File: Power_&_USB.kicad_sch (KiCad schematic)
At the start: 36 parts, among them J1 UJ20-C-H-G-SMT-1-P16-TR, U1 TPS62840YBGR, U2 TPS62840YBGR, U4 FT232HPQ

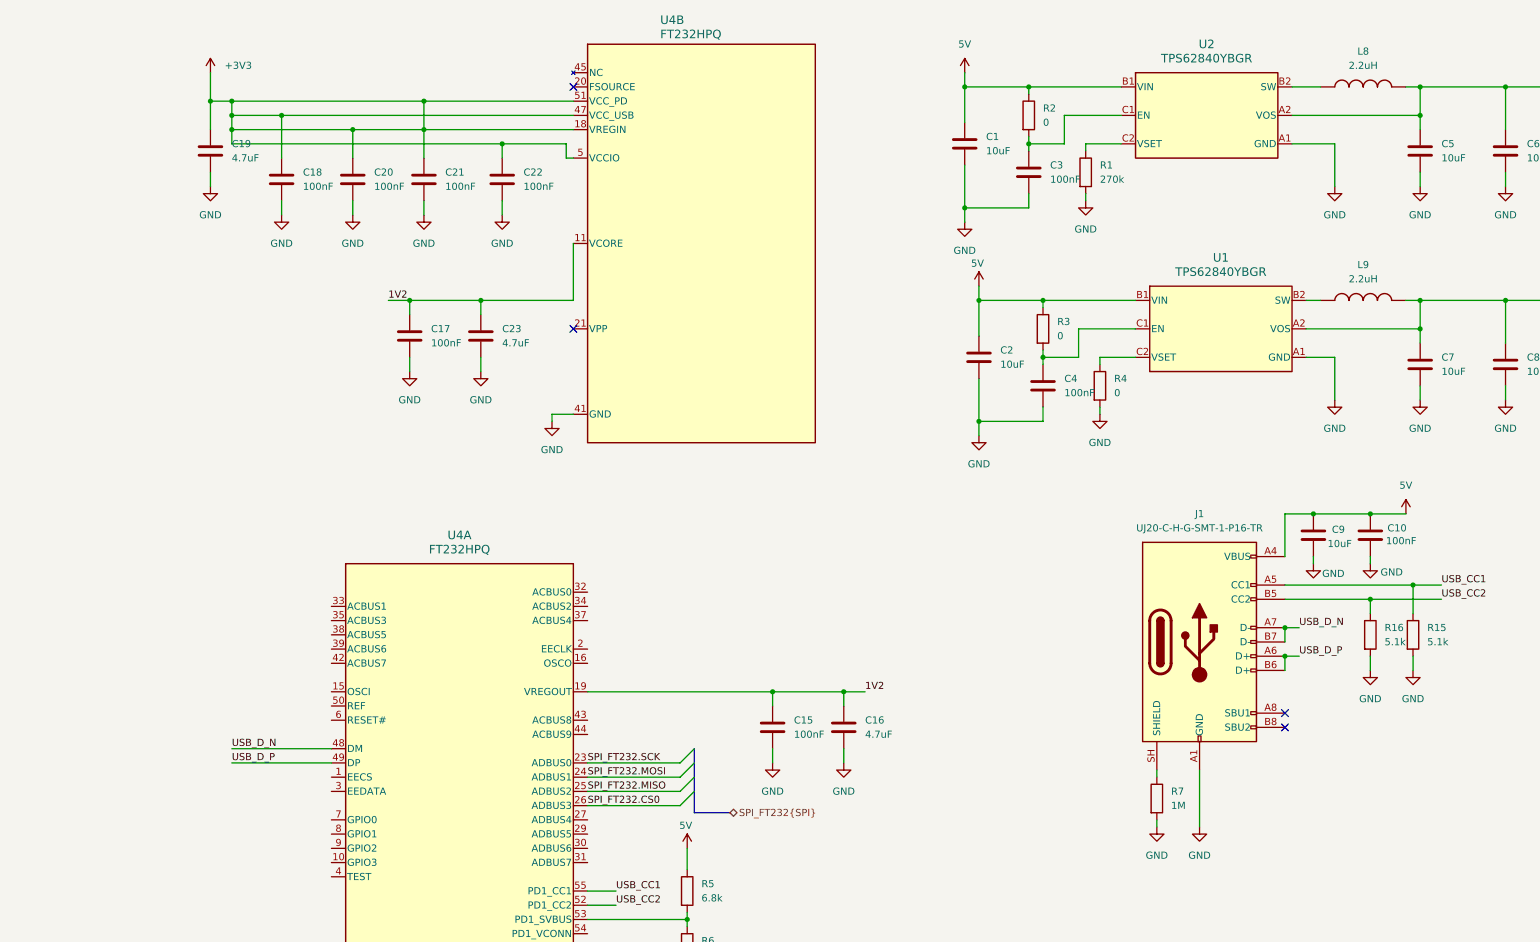
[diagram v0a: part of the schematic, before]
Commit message: added schematics comments of review 1
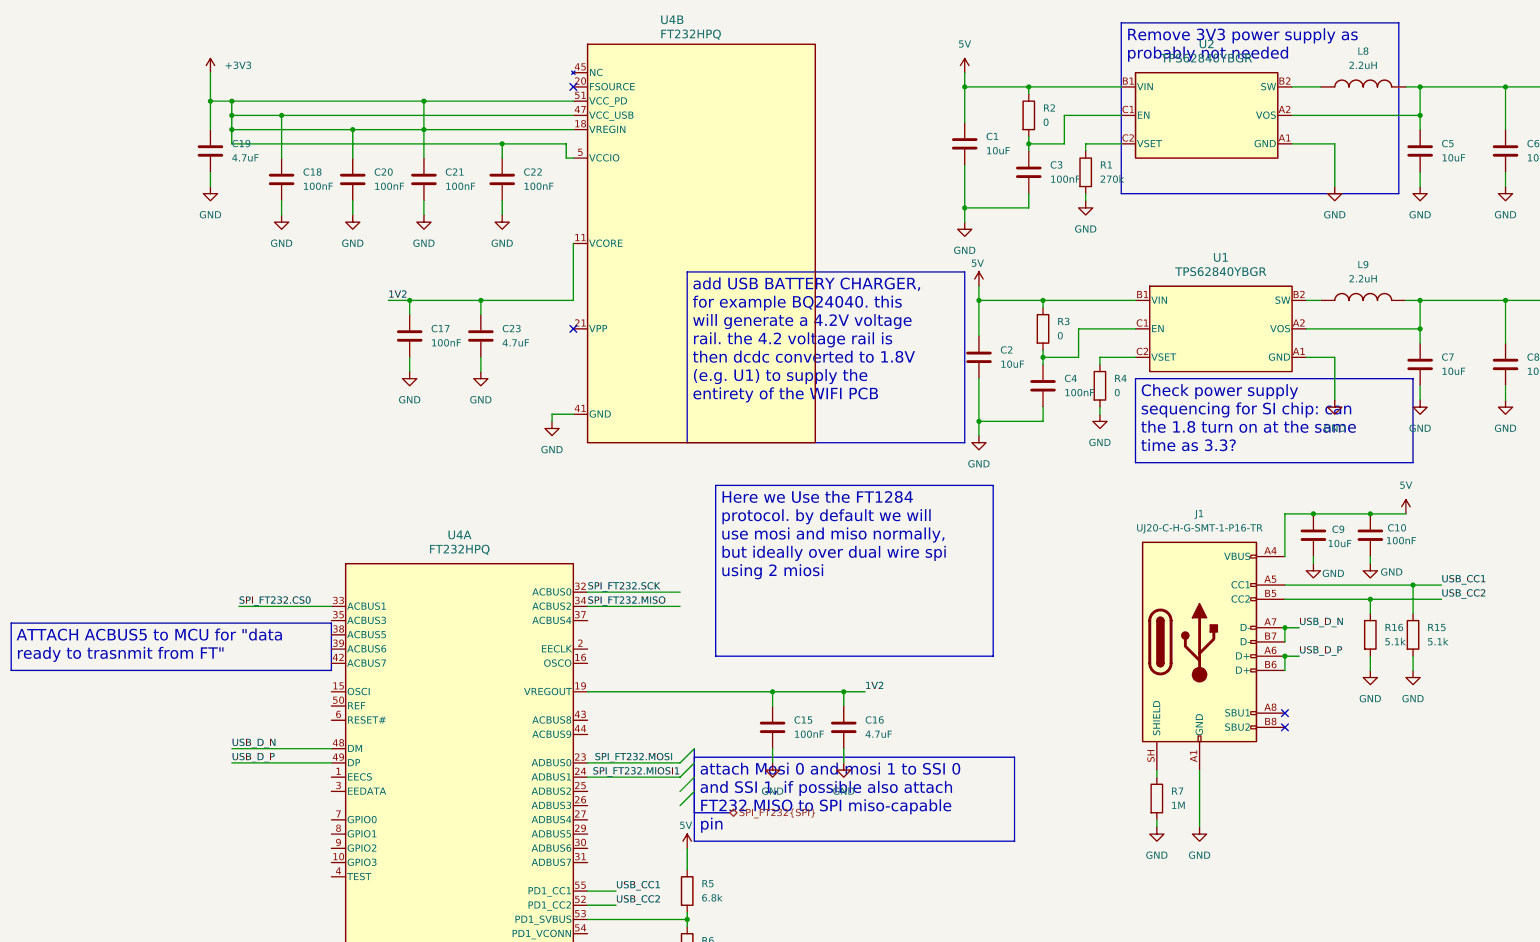
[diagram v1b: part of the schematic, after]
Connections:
- net SPI_FT232.CS0: now also U4.33 (ACBUS1); no longer U4.26 (ADBUS3)
- net SPI_FT232.MISO: now also U4.34 (ACBUS2); no longer U4.25 (ADBUS2)
- net SPI_FT232.MOSI: now also U4.23 (ADBUS0); no longer U4.24 (ADBUS1)
- net SPI_FT232.SCK: now also U4.32 (ACBUS0); no longer U4.23 (ADBUS0)
- new net SPI_FT232.MIOSI1: U4.24 (ADBUS1)

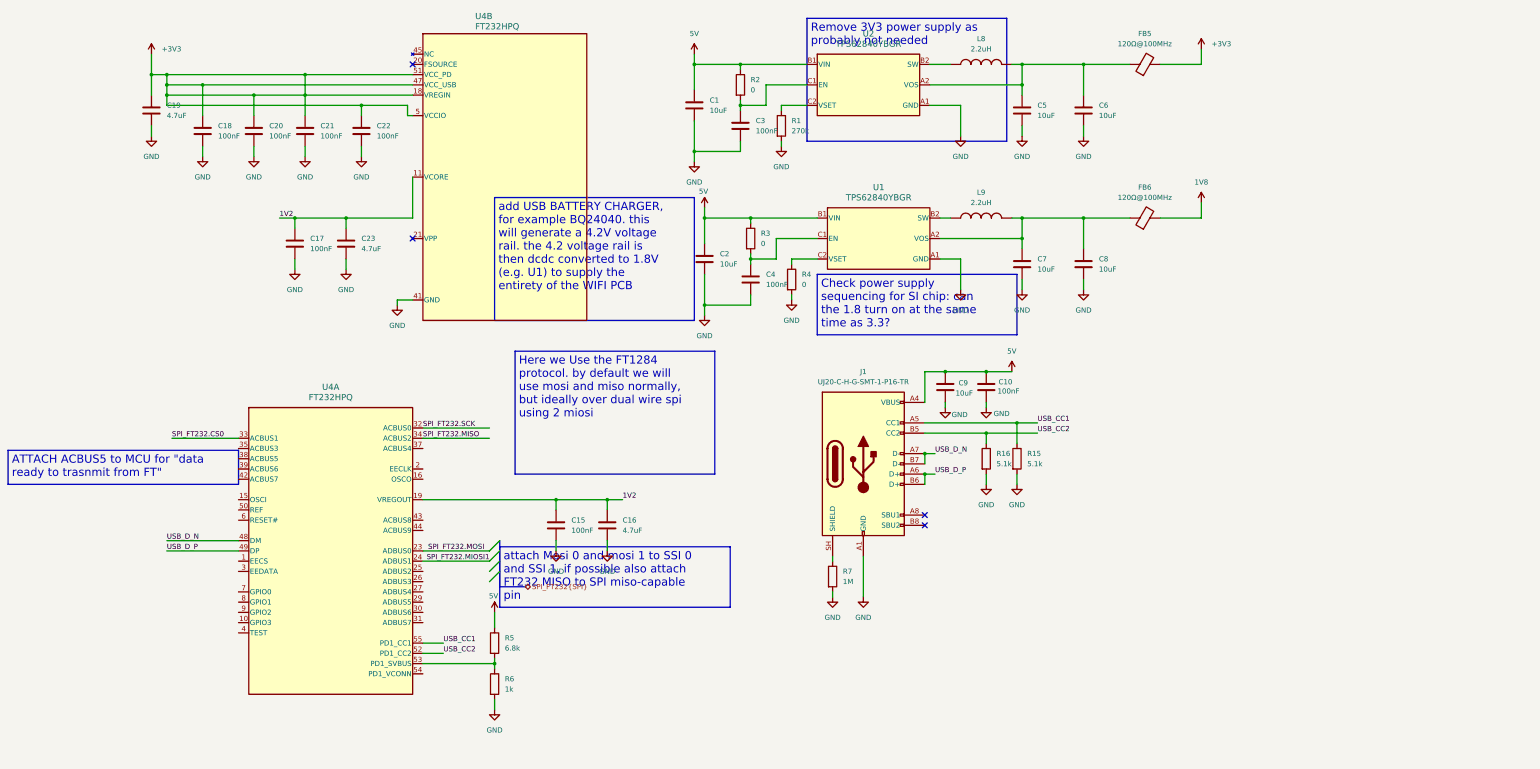
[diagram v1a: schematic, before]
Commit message: changes after first review: add lvl shifters, board at 1v8, new power tree
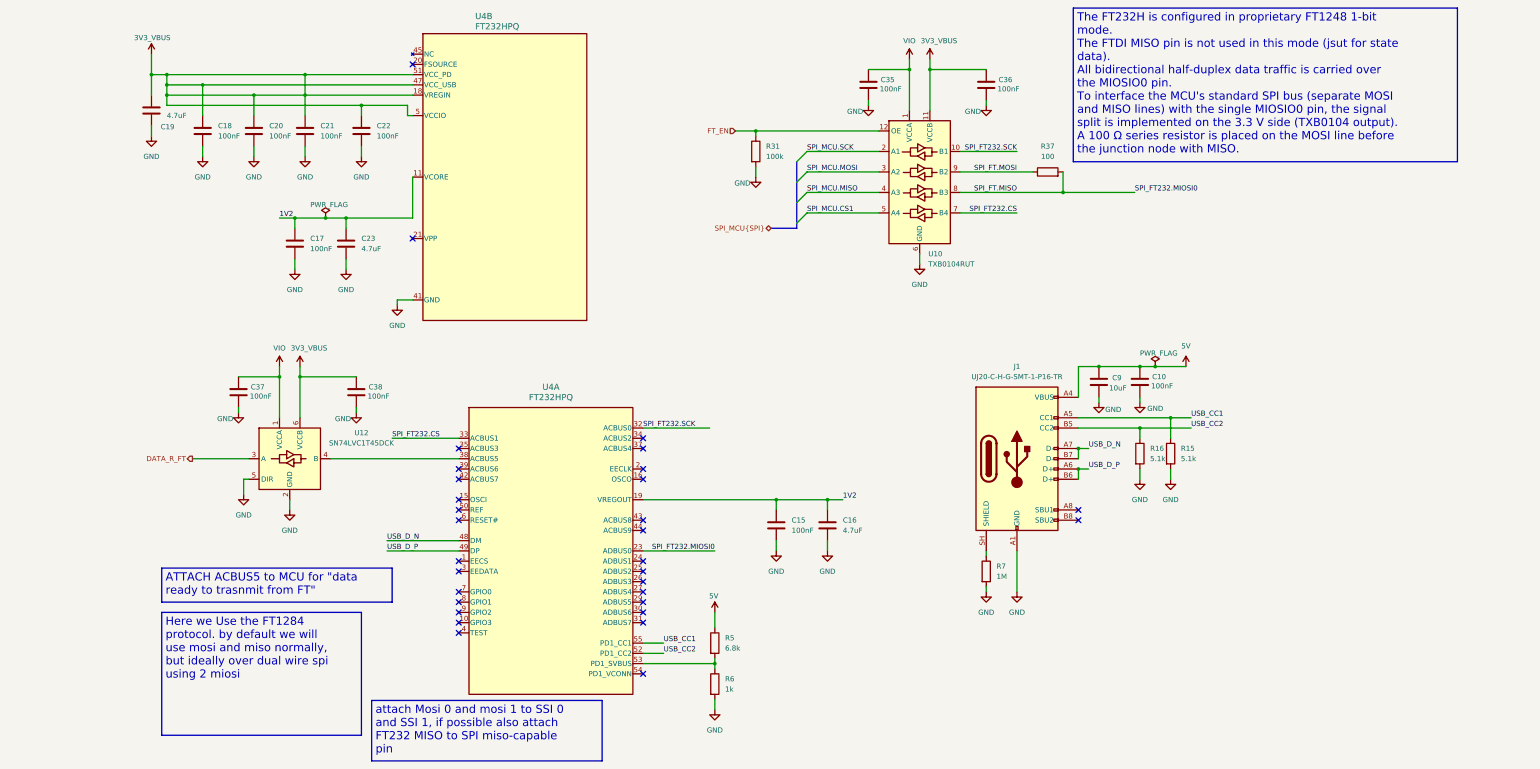
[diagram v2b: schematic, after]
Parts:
- removed C1, C2, C5, C6, C7, C8: 10uF, Capacitor_SMD:C_0603_1608Metric, symbol #dzdb:g_cap/C-10u-0603
- removed C3, C4: 100nF, Capacitor_SMD:C_0402_1005Metric, symbol #dzdb:g_cap/C-100n-0402
- removed FB5, FB6: 120Ω@100MHz, dz_ind:BLM15KD121SN1D, symbol #dzdb:s_ind/L-FB-120R-1.5A-0402
- removed L8, L9: 2.2uH, dz_ind:DFE2MCAH2R2MJ0L, symbol #dzdb:s_ind/L-2.2uH-1.4A-0806
- removed R1: 270k, Resistor_SMD:R_0402_1005Metric, symbol #dzdb:g_res/R-270k-0402
- removed R2, R3, R4: 0, Resistor_SMD:R_0402_1005Metric, symbol #dzdb:g_res/R-0-0402
- removed U1, U2: TPS62840YBGR, dz_pwr:DSBGA6_1P4XP9_TEX, symbol #dzdb:s_pwr/P-TI-TPS62840YBGR
- added C35, C36, C37, C38: 100nF, Capacitor_SMD:C_0603_1608Metric, symbol #dzdb:g_cap/C-100n-0603
- added R31: 100k, Resistor_SMD:R_0402_1005Metric, symbol #dzdb:g_res/R-100k-0402
- added R37: 100, Resistor_SMD:R_0402_1005Metric, symbol #dzdb:g_res/R-100-0402
- added U10: TXB0104RUT, Package_DFN_QFN:Texas_R-PUQFN-N12, symbol Logic_LevelTranslator:TXB0104RUT
- added U12: SN74LVC1T45DCK, Package_TO_SOT_SMD:SOT-363_SC-70-6, symbol Logic_LevelTranslator:SN74LVC1T45DCK
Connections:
- net GND: now also U4.57 (GND), C35.2, C36.2, C37.2, C38.2, R31.2, U10.6 (GND), U12.2 (GND), U12.5 (DIR)
- net SPI_FT232.SCK: now also U10.10 (B1)
- net at U4.38 (ACBUS5): now also U12.4 (B)
- net +3V3 renamed 3V3_VBUS
- net 3V3_VBUS: now also C36.1, C38.1, U10.11 (VCCB), U12.6 (VCCB)
- net SPI_FT232.CS0 renamed SPI_FT232.CS
- net SPI_FT232.CS: now also U10.7 (B4)
- net SPI_FT232.MIOSI1: no longer names the net of U4.24 (ADBUS1)
- net SPI_FT232.MISO: no longer names the net of U4.34 (ACBUS2)
- net SPI_FT232.MOSI renamed SPI_FT.MISO
- net SPI_FT.MISO: now also R37.2, U10.8 (B3)
- new net DATA_R_FT: U12.3 (A)
- new net FT_EN: R31.1, U10.12 (OE)
- new net SPI_FT.MOSI: R37.1, U10.9 (B2)
- new net SPI_MCU.CS1: U10.5 (A4)
- new net SPI_MCU.MISO: U10.4 (A3)
- new net SPI_MCU.MOSI: U10.3 (A2)
- new net SPI_MCU.SCK: U10.2 (A1)
- new net VIO: C35.1, C37.1, U10.1 (VCCA), U12.1 (VCCA)
- no-connect marks 4 -> 31
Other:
- moved on the sheet: C10, C15, C16, C9, J1, R15, R16, R5, R6, R7, U4A

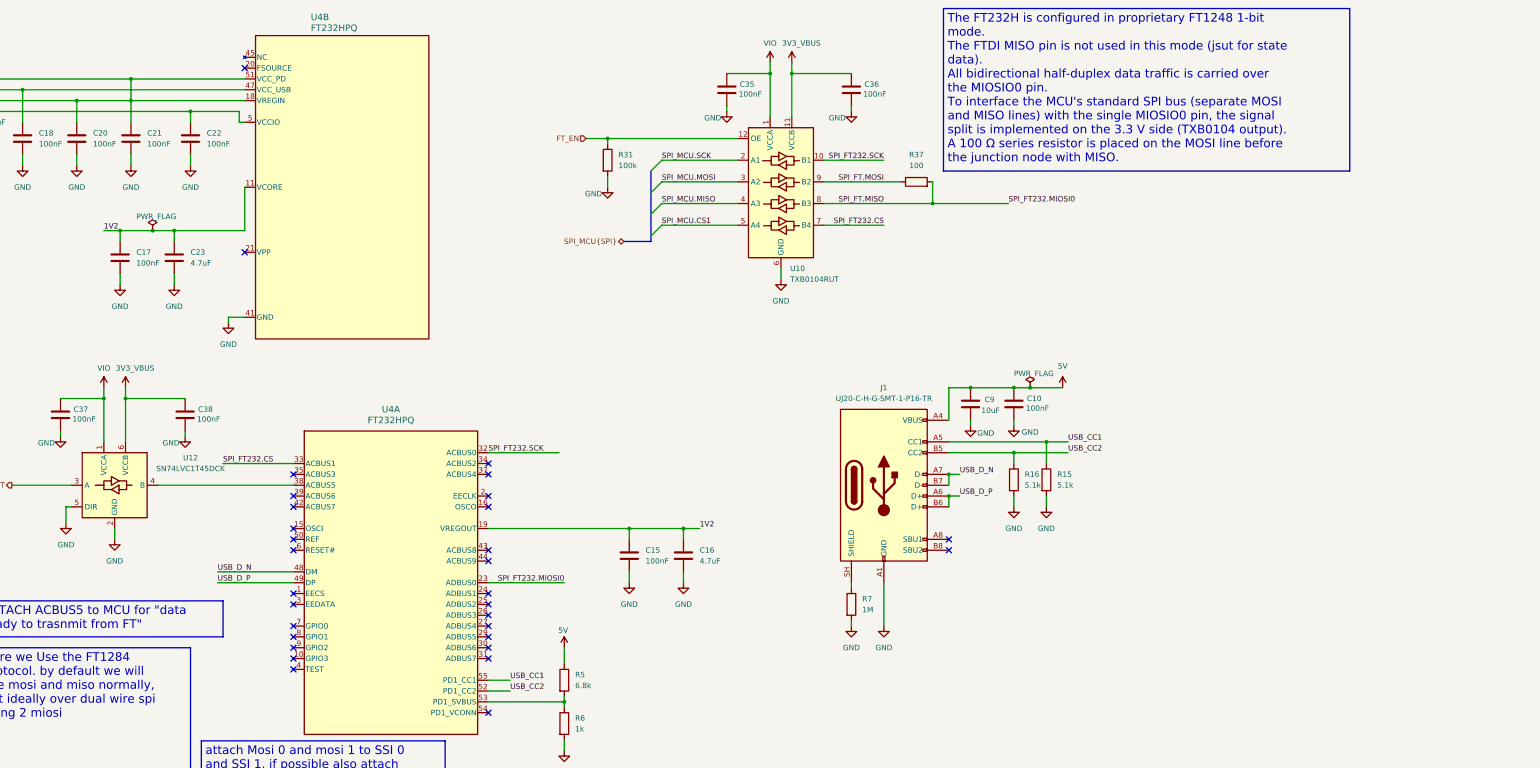
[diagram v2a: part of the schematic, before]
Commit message: updated schematic and initial pcb placement
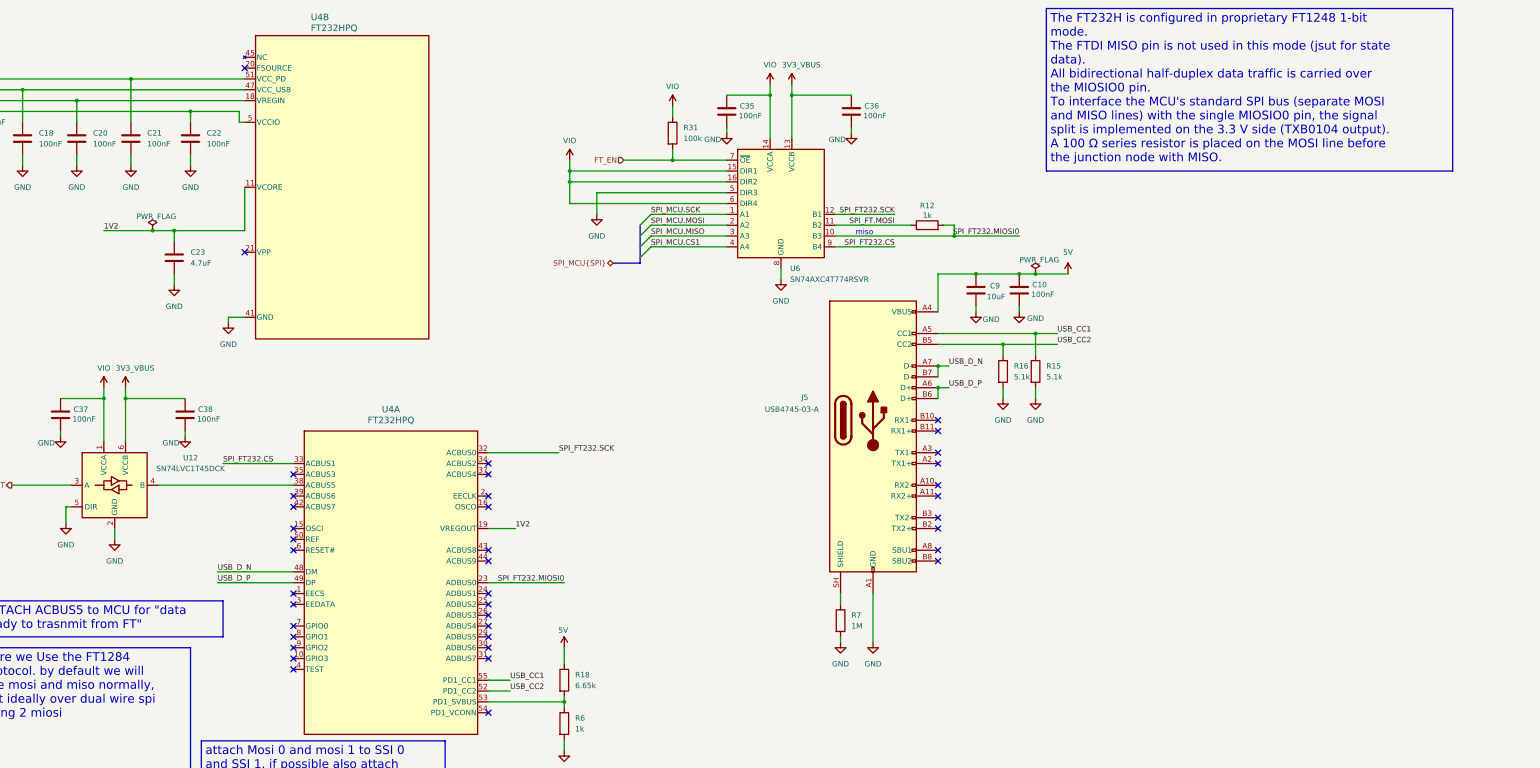
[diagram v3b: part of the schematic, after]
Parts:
- removed C15, C17: 100nF, Capacitor_SMD:C_0402_1005Metric, symbol #dzdb:g_cap/C-100n-0402
- removed C16: 4.7uF, Capacitor_SMD:C_0402_1005Metric, symbol #dzdb:g_cap/C-4.7u-0402
- removed J1: UJ20-C-H-G-SMT-1-P16-TR, Connector_USB:USB_C_Receptacle_GCT_USB4105-xx-A_16P_TopMnt_Horizontal, symbol #dzdb:s_con/CON-USB-USBC-2.0-HORIZONTAL
- removed R37: 100, Resistor_SMD:R_0402_1005Metric, symbol #dzdb:g_res/R-100-0402
- removed R5: 6.8k, Resistor_SMD:R_0402_1005Metric, symbol #dzdb:g_res/R-6k8-0402
- removed U10: TXB0104RUT, Package_DFN_QFN:Texas_R-PUQFN-N12, symbol Logic_LevelTranslator:TXB0104RUT
- added J5: USB4745-03-A, dz_con:GTC_USB4745, symbol #dzdb:s_con/CON-GCT-USB4745-03-A
- added R12: 1k, Resistor_SMD:R_0402_1005Metric, symbol #dzdb:g_res/R-1k-0402
- added R18: 6.65k, Resistor_SMD:R_0402_1005Metric, symbol #dzdb:g_res/R-6k65-0402
- added U6: SN74AXC4T774RSVR, Package_DFN_QFN:UQFN-16_1.8x2.6mm_P0.4mm, symbol #dzdb:s_comm/COMM-TI-SN74AXC4T774RSVR
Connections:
- net 3V3_VBUS: now also U6.13 (VCCB)
- net 5V: now also J5.A4 (VBUS), J5.A9 (VBUS), J5.B4 (VBUS), J5.B9 (VBUS), R18.1
- net FT_EN: now also R31.2, U6.7 (~{OE}); no longer R31.1
- net GND: now also J5.A1 (GND), J5.A12 (GND), J5.B1 (GND), J5.B12 (GND), U6.5 (DIR3), U6.8 (GND); no longer R31.2
- net SPI_FT.MOSI: now also R12.1, U6.11 (B2)
- net SPI_FT232.CS: now also U6.9 (B4)
- net SPI_FT232.SCK: now also U6.12 (B1)
- net SPI_MCU.CS1: now also U6.4 (A4)
- net SPI_MCU.MISO: now also U6.3 (A3)
- net SPI_MCU.MOSI: now also U6.2 (A2)
- net SPI_MCU.SCK: now also U6.1 (A1)
- net USB_CC1: now also J5.A5 (CC1)
- net USB_CC2: now also J5.B5 (CC2)
- net USB_D_N: now also J5.A7 (D-), J5.B7 (D-)
- net USB_D_P: now also J5.A6 (D+), J5.B6 (D+)
- net VIO: now also R31.1, U6.14 (VCCA), U6.15 (DIR1), U6.16 (DIR2), U6.6 (DIR4)
- net at R7.1: now also J5.SH (SHIELD)
- net at R6.1, U4.53 (PD1_SVBUS): now also R18.2
- net SPI_FT.MISO renamed SPI_FT232.MIOSI0
- net SPI_FT232.MIOSI0: now also R12.2, U6.10 (B3)
- no-connect marks 31 -> 39
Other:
- note added: "miso"
- moved on the sheet: C10, C35, C36, C9, R15, R16, R31, R7
